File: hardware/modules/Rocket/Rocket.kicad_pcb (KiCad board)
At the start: 2 copper layers, 35 x 107 mm, 103 parts, among them J101 Conn_01x03, J102 Ext Switch, J103 LiPo, J104 Conn_01x02, J105 UFL, SW101 RESET_sw, SW102 SW_Push_DPDT, U101 TPS3820, U102 ESP32-S3-WROOM-1, U103 TPS2116DRL, U104 MCP73871-1CC, U105 INA226, U106 INA226, U107 TPS63070RNMR, U108 INA226, U109 PCF8563T, U110 SAM-M10Q, U111 E220-900T22S(JP), U113 BMI088, U114 QMC5883L, Y101 Crystal

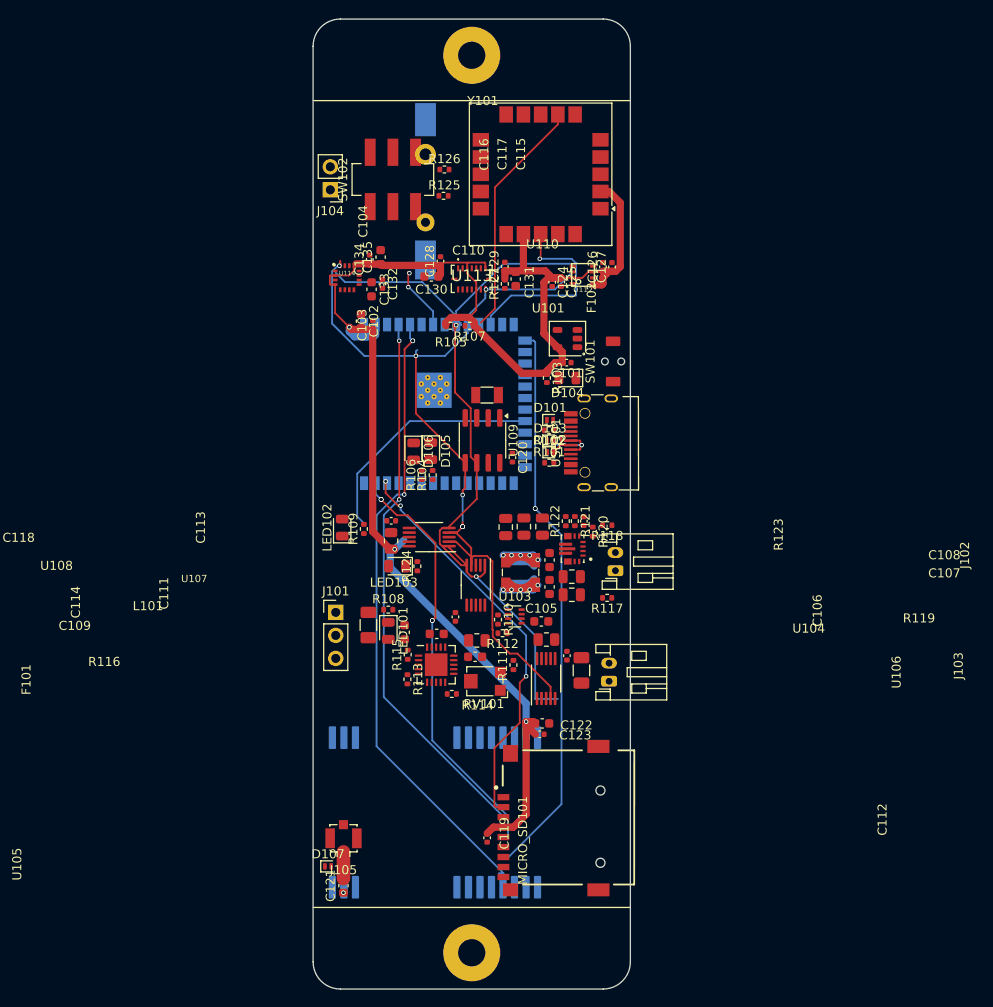
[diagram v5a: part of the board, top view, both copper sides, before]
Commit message: あと11箇所未配線です
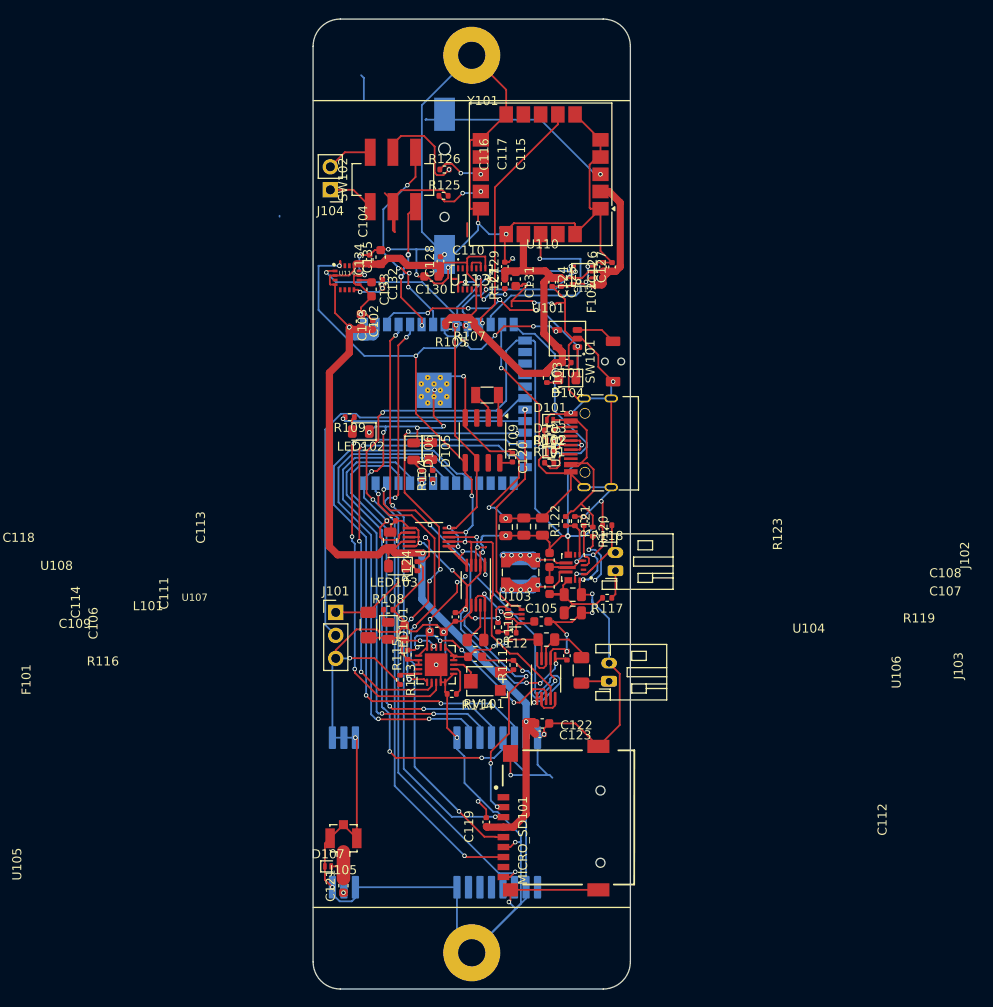
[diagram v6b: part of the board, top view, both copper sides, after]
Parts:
- moved R109 12.4 mm to (124.0, 86.9), turned to 180 degrees
- moved LED102 10.8 mm to (125.3, 88.5), turned to 180 degrees
- moved BT101 2.18 mm to (134.5, 61.1)
- moved U107 2.07 mm to (148.7, 103.5)
- moved C107 1.99 mm to (148.7, 108.5)
- moved C108 1.99 mm to (148.7, 106.5)
- moved C119 1.74 mm to (139.1, 131.6), turned to 90 degrees
- moved R112 0.99 mm to (141.9, 110.7)
- moved R110 0.84 mm to (140.4, 110.1)
- moved R113 0.81 mm to (129.6, 115.9)
- moved C109 0.23 mm to (133.6, 110.6)
- moved R116 0.16 mm to (137.9, 111.5)
- moved R123 0.11 mm to (128.5, 100.5)
- turned C106 to -90 degrees
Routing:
- net GND: track 0.07 -> 571.7 mm, vias 0 -> 54
- net VBUS: track 0.07 -> 108.2 mm, vias 0 -> 9
- net /AUX: track 0.00 -> 63.1 mm, vias 0 -> 2
- net /M0: track 0.00 -> 56.5 mm, vias 0 -> 2
- net /RTX0: track 0.00 -> 56.1 mm, vias 0 -> 2
- net /STAT1: track 0.00 -> 56.0 mm, vias 0 -> 3
- net /M1: track 0.00 -> 54.8 mm, vias 0 -> 2
- net /STAT2: track 0.00 -> 52.7 mm, vias 0 -> 3
- net /TRX0: track 0.00 -> 47.9 mm, vias 0 -> 2
- net /DetL: track 0.00 -> 47.0 mm
- net /PG: track 0.00 -> 45.8 mm, vias 0 -> 6
- net /MISO: track 61.7 -> 104.3 mm, vias 2 -> 3
- net RESET: track 0.00 -> 31.7 mm, vias 0 -> 7
- net /ST: track 0.00 -> 25.4 mm, vias 0 -> 1
- net /GPS SAM-M10Q2/BUCKUP: track 0.14 -> 22.5 mm, vias 0 -> 1
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
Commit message: ロケット電装修正
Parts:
- removed C121: 100p, Capacitor_SMD:C_0603_1608Metric
- removed D107: ESD9B5.0ST5G, Diode_SMD:D_SOD-882
- removed J105: UFL, Connector_Coaxial:U.FL_Molex_MCRF_73412-0110_Vertical
- removed SW102: SW_Push_DPDT, WOBCLibrary:IS-2245S-G
- added D201: D, Diode_SMD:D_SOD-323, F.Cu at (149.7, 95.5)
- added D301: D, Diode_SMD:D_SOD-323, F.Cu at (149.7, 98.9)
- added D401: D, Diode_SMD:D_SOD-323, F.Cu at (139.1, 81.2)
- added D402: D, Diode_SMD:D_SOD-323, F.Cu at (141.1, 81.3)
- added J501: Conn_01x02, Connector_PinHeader_1.27mm:PinHeader_1x02_P1.27mm_Vertical, F.Cu at (125.2, 63.1)
- added SW201: Boot_sw, WOBCLibrary:TVAF06-A020B-R, F.Cu at (145.7, 97.0)
- C119: footprint Capacitor_SMD:C_0402_1005Metric -> Capacitor_SMD:C_0603_1608Metric
- C122: value 10u -> 10uF
- C123: value 100n -> 100nF
- C124, C127: value 10μF -> 10uF; footprint Capacitor_SMD:C_0402_1005Metric -> Capacitor_SMD:C_0603_1608Metric
- C130, C131, C135: value 10μF -> 10uF
- C132: value 0.22μF -> 0.22uF
- C133: value 4.7μF -> 4.7uF
- D101, D102, D103: footprint Diode_SMD:D_SOD-882 -> Diode_SMD:D_SOD-882D
- J104: footprint Connector_PinHeader_2.54mm:PinHeader_1x02_P2.54mm_Vertical -> Connector_PinHeader_1.27mm:PinHeader_1x02_P1.27mm_Vertical
- U113: footprint WOBClibraries:BMI088 -> WOBCLibrary:BMI088
- moved J101 31.8 mm to (152.5, 97.9)
- moved R117 7.40 mm to (145.7, 109.9)
- moved R118 6.60 mm to (148.9, 104.4), turned to 0 degrees
- moved J102 6.31 mm to (150.3, 109.4)
- moved C105 5.78 mm to (139.4, 109.2), turned to 180 degrees
- moved J104 4.02 mm to (125.1, 59.4), turned to 0 degrees
- moved R120 3.98 mm to (149.5, 103.3), turned to 180 degrees
- moved U105 3.96 mm to (134.4, 103.7)
- moved R116 3.96 mm to (135.9, 108.1)
- moved C113 3.50 mm to (149.0, 101.8)
- moved C115 3.50 mm to (141.8, 99.0)
- moved C116 3.50 mm to (137.8, 99.0)
- moved C117 3.50 mm to (139.8, 99.0)
- moved F102 3.01 mm to (147.4, 116.9)
- moved C106 2.95 mm to (138.2, 107.4), turned to 90 degrees
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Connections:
- BT101 pad 1: /GPS SAM-M10Q2/BUCKUP -> +BATT
- C106 pad 1: VBUS -> VPP
- C112 pad 1: VBUS -> VPP
- C120 pad 2: +BATT -> Net-(D401-K)
- D101 pad 2: VBUS -> Net-(D101-A2)
- J101 pad 1: VBUS -> Net-(D301-A)
- J104 pad 2: Net-(J104-Pin_2) -> /RTX1
- R116 pad 1: Net-(U105-Vbus) -> VPP
- R125 pad 2: Net-(R125-Pad2) -> Net-(J104-Pin_1)
- R126 pad 2: Net-(R126-Pad2) -> /RTX1
- U102 pad 27: unconnected-(U102-GPIO0/BOOT-Pad27) -> Net-(U102-GPIO0/BOOT)
- U102 pad 32: /M0 -> /M1
- U102 pad 33: /M1 -> /M0
- U103 pad 2: Net-(U105-Vbus) -> VPP
- U103 pad 7: Net-(U105-Vbus) -> VPP
- U105 pad 10: Net-(U105-Vbus) -> VPP
- U105 pad 2: VBUS -> VPP
- U105 pad 6: VBUS -> VPP
- U105 pad 8: Net-(U105-Vbus) -> VPP
- U106 pad 6: VBUS -> VPP
- U109 pad 8: +BATT -> Net-(D401-K)
- U110 pad 3: /GPS SAM-M10Q2/BUCKUP -> +BATT
- U111 pad 21: Net-(U111-ANT) -> unconnected-(U111-ANT-Pad21)
- USB101 pad A4: VBUS -> Net-(D101-A2)
- USB101 pad A9: VBUS -> Net-(D101-A2)
- USB101 pad B4: VBUS -> Net-(D101-A2)
- USB101 pad B9: VBUS -> Net-(D101-A2)
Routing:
- net VBUS: track 108.2 -> 61.6 mm, vias 9 -> 2
- net +BATT: track 1.43 -> 38.7 mm, vias 0 -> 4
- net VDD: track 188.0 -> 221.9 mm, vias 3 -> 6
- net VPP: track 0.00 -> 30.3 mm, vias 0 -> 2
- net /DetL: track 47.0 -> 20.2 mm
- net GND: track 571.7 -> 597.7 mm, vias 54 -> 366
- net Net-(D101-A2): track 0.00 -> 24.8 mm
- net /AUX: track 63.1 -> 39.7 mm, vias 2 -> 0
- net /MISO: track 104.3 -> 81.2 mm
- net /GPS SAM-M10Q2/BUCKUP: track 22.5 -> 0.00 mm, vias 1 -> 0
- net /M0: track 56.5 -> 36.6 mm, vias 2 -> 0
- net /M1: track 54.8 -> 37.3 mm, vias 2 -> 0
- net Net-(R125-Pad2): track 15.3 -> 0.00 mm
- net Net-(D401-K): track 0.00 -> 13.8 mm
- net Net-(U103-MODE): track 15.4 -> 28.5 mm, vias 4 -> 0
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- added copper zone on B.Cu, net GND
- added copper zone on F.Cu, net GND

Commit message: シルク追加
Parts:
- moved BT101 1.19 mm to (134.3, 62.2)
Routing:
- net /TRX1: track 16.6 -> 18.3 mm
- net GND: track 597.7 -> 599.1 mm, vias 366 -> 364
- net +BATT: track 38.7 -> 39.5 mm
- net /TimePulse: track 35.8 -> 36.4 mm
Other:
- board text added: "CHARGE"
- board text added: "ERROR"
- board text added: "GNSS SET"
- board text added: "RESET"
- board text added: "STAT"
- board text added: "Switch"
- board text added: "USB Power"
- board text added: "VDD/Det/GND"
